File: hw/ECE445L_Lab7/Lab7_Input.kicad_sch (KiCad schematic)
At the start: 5 parts, among them SW1 UP, SW2 DOWN, SW3 LEFT, SW4 RIGHT, SW5 MODE

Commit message: Updated hardware schematic
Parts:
- added R44, R45, R46, R47, R48: 10k, symbol Device:R
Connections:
- net SW_DOWN renamed PB1
- net PB1: now also R45.2
- net SW_LEFT renamed PB2
- net PB2: now also R46.2
- net SW_MODE renamed PB4
- net PB4: now also R48.2
- net SW_RIGHT renamed PB3
- net PB3: now also R47.2
- net SW_UP renamed PB0
- net PB0: now also R44.2
- new net +3V3: R44.1, R45.1, R46.1, R47.1, R48.1
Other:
- moved on the sheet: SW1, SW2, SW3, SW4, SW5

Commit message: More Updates to hardware
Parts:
- added R49, R50, R51, R52, R53, R54, R55: 10k, ECE445L:Potentiometer, symbol ECE445L:Potentiometer
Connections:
- net +3V3: now also R49.1, R50.1, R51.1, R52.1, R53.1, R54.1, R55.1
- net GND: now also R49.3, R50.3, R51.3, R52.3, R53.3, R54.3, R55.3
- new net PE1: R51.2, R52.2, R53.2, R54.2, R55.2
- new net PE2: R50.2
- new net PE3: R49.2
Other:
- note added: "Bass"
- note added: "Distortion Knob"
- note added: "Flanger Potentiometers"
- note added: "Mid"
- note added: "Treble"
- note added: "Volume"

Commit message: Lab7A Schematic and BOM - Ashton
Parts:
- added R80: 10k, ECE445L:Potentiometer, symbol ECE445L:Potentiometer
- added R81: 10k, symbol Device:R
- added SW6: Delay, ECE445L:SW_PUSH_6mm, symbol ECE445L:SW_Push
- SW1: value UP -> Pause
- SW2: value DOWN -> LCDMode
- SW3: value LEFT -> Flanger
- SW4: value RIGHT -> Distortion
- SW5: value MODE -> Reverb
- renumbered R44 to R65, R45 to R66, R46 to R67, R47 to R68, R48 to R69, R49 to R70, R50 to R71, R51 to R72, R52 to R73, R53 to R74, R54 to R75, R55 to R76
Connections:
- net +3V3: now also R80.1, R81.1
- net GND: now also R80.3, SW6.1
- net PE1: no longer R73.2, R74.2, R75.2, R76.2
- new net PC7: R81.2, SW6.2
- new net PD1: R76.2, R80.2
- new net PD2: R75.2
- new net PD3: R74.2
- new net PE0: R73.2
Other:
- note added: "Delay"

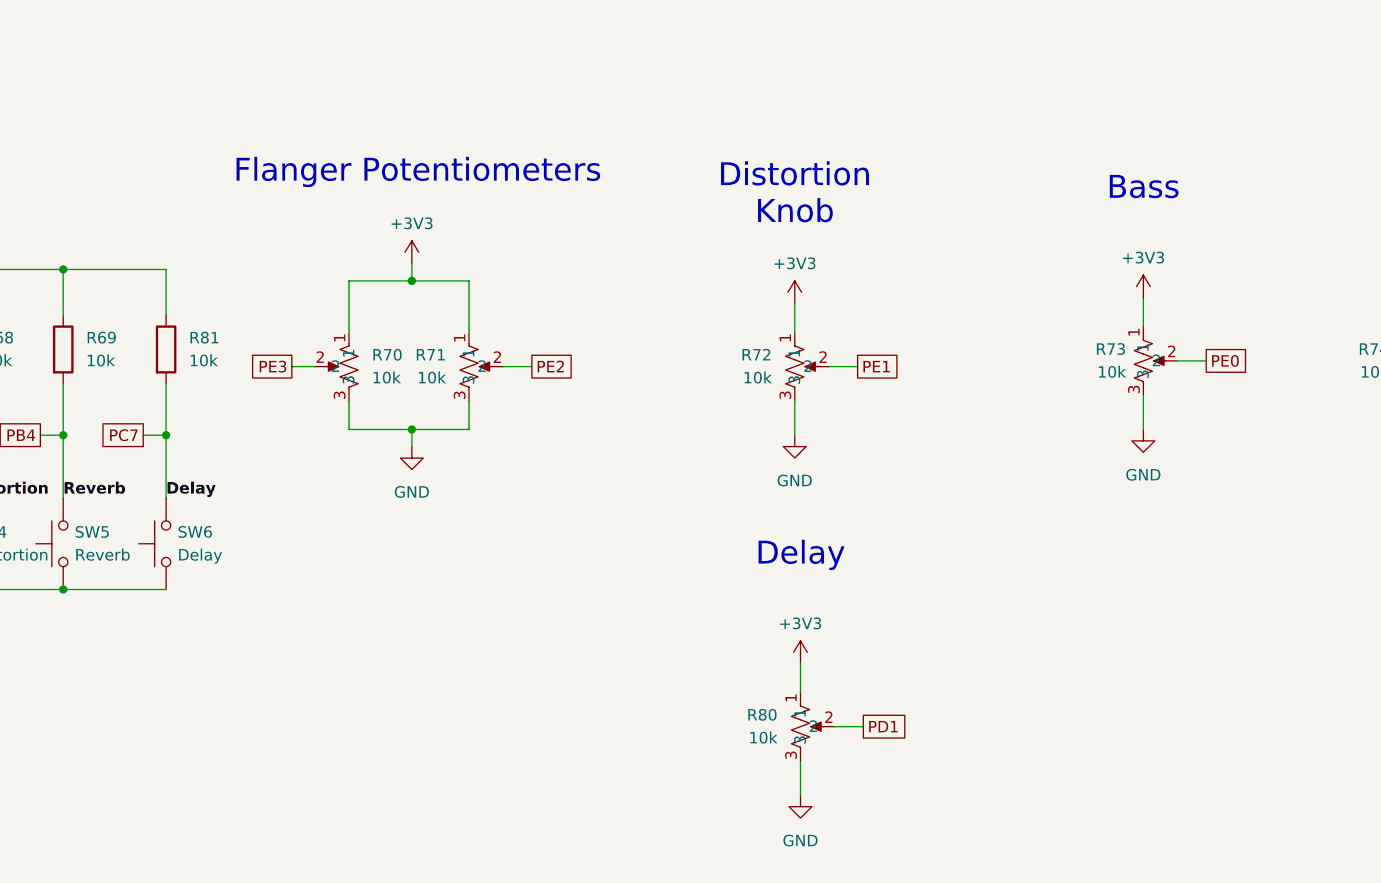
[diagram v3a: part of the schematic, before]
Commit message: Made changers to the schematic, updated bom, and created priliminary layout for the PCB. Ready for 7B Prep!
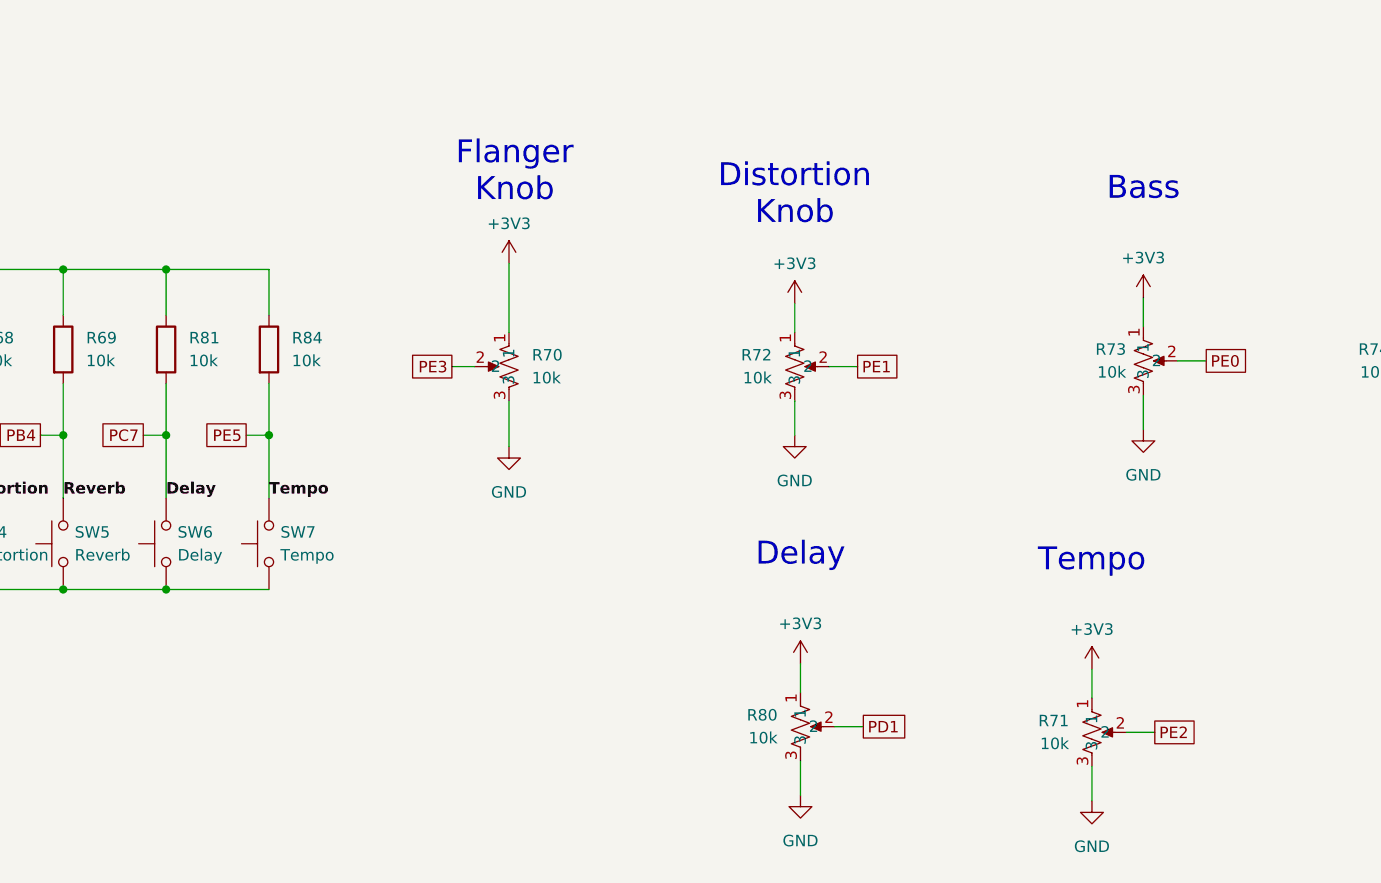
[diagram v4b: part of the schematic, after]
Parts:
- added R84: 10k, Resistor_SMD:R_0603_1608Metric, symbol Device:R
- added SW7: Tempo, ECE445L:SW_PUSH_6mm, symbol ECE445L:SW_Push
- R65, R66, R67, R68, R69, R81: footprint (none) -> Resistor_SMD:R_0603_1608Metric
- R70, R71, R72, R73, R74, R75, R76, R80: footprint ECE445L:Potentiometer -> ECE445L:P120PK-Y25BR10K
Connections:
- net +3V3: now also R84.1
- net GND: now also SW7.1
- new net PE5: R84.2, SW7.2
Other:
- note added: "Flanger Knob"
- note added: "Tempo"
- note removed: "Flanger Potentiometers"
- moved on the sheet: R70, R71

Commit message: Rough draft layout - need to remove tm4c chip
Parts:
- R70: renamed from R65; footprint Resistor_SMD:R_0603_1608Metric -> Resistor_SMD:R_0603_1608Metric_Pad0.98x0.95mm_HandSolder
- R71: renamed from R66; footprint Resistor_SMD:R_0603_1608Metric -> Resistor_SMD:R_0603_1608Metric_Pad0.98x0.95mm_HandSolder
- R72: renamed from R67; footprint Resistor_SMD:R_0603_1608Metric -> Resistor_SMD:R_0603_1608Metric_Pad0.98x0.95mm_HandSolder
- R73: renamed from R68; footprint Resistor_SMD:R_0603_1608Metric -> Resistor_SMD:R_0603_1608Metric_Pad0.98x0.95mm_HandSolder
- R74: renamed from R69; footprint Resistor_SMD:R_0603_1608Metric -> Resistor_SMD:R_0603_1608Metric_Pad0.98x0.95mm_HandSolder
- R75: renamed from R81; footprint Resistor_SMD:R_0603_1608Metric -> Resistor_SMD:R_0603_1608Metric_Pad0.98x0.95mm_HandSolder
- R76: renamed from R84; footprint Resistor_SMD:R_0603_1608Metric -> Resistor_SMD:R_0603_1608Metric_Pad0.98x0.95mm_HandSolder
- renumbered R70 to R77, R72 to R78, R80 to R79, R71 to R80, R73 to R81, R74 to R82, R75 to R83, R76 to R84, SW1 to SW2, SW2 to SW3, SW3 to SW4, SW4 to SW5, SW5 to SW6, SW6 to SW7, SW7 to SW8
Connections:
- net PD1: no longer R79.2
- net PB0 renamed PF0
- net PB1 renamed PF1
- net PB2 renamed PF2
- net PB3 renamed PF3
- net PB4 renamed PF4
- new net PE4: R79.2
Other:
- company: (none) -> The University of Texas at Austin
- title: (none) -> ECE 445L Lab7

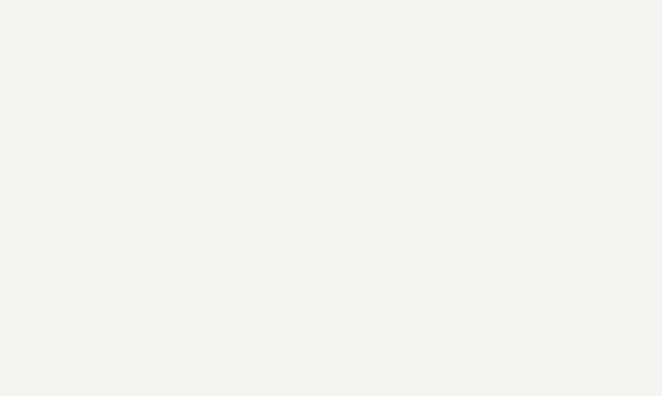
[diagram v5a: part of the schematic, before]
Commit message: Added current consumption to schematic
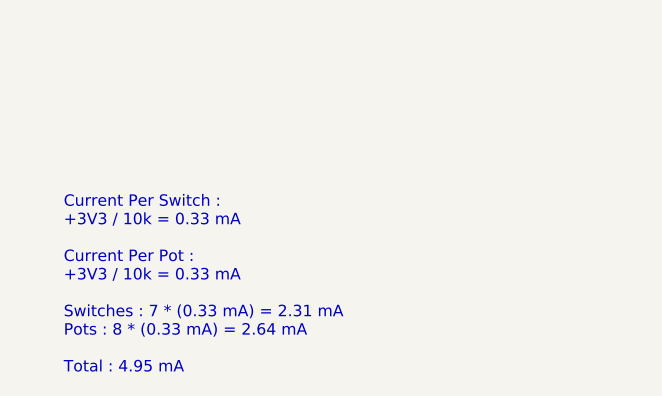
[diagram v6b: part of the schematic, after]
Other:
- note added: "Current Per Switch : +3V3 / 10k = 0.33 mA Current Per Pot : +3V3 / 10k = 0.33 mA Switches : 7 * (0.33 mA) = 2.31 mA Pots : 8 * (0.33 mA) = 2.64 mA Total : 4.95 mA"
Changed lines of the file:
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@@
 		(comment 1 "Drawn By Ashton Knecht - atk836")
+	)
+	(text "Current Per Switch :\n+3V3 / 10k = 0.33 mA\n\nCurrent Per Pot :\n+3V3 / 10k = 0.33 mA\n\nSwitches : 7 * (0.33 mA) = 2.31 mA\nPots : 8 * (0.33 mA) = 2.64 mA\n\nTotal : 4.95 mA"
+		(exclude_from_sim no)
+		(at 36.195 182.88 0)
+		(effects
+			(font
+				(size 1.27 1.27)
+			)
+			(justify left)
+		)
 	)
 	(text "Mid"

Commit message: Updated lab7a report
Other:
- note added: "Inputs Current Consumption Current Per Switch : +3V3 / 10k = 0.33 mA Current Per Pot : +3V3 / 10k = 0.33 mA Switches : 7 * (0.33 mA) = 2.31 mA Pots : 8 * (0.33 mA) = 2.64 mA Total : 4.95 mA"
- note removed: "Current Per Switch : +3V3 / 10k = 0.33 mA Current Per Pot : +3V3 / 10k = 0.33 mA Switches : 7 * (0.33 mA) = 2.31 mA Pots : 8 * (0.33 mA) = 2.64 mA Total : 4.95 mA"
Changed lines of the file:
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@@
 		(comment 1 "Drawn By Ashton Knecht - atk836")
 	)
-	(text "Current Per Switch :\n+3V3 / 10k = 0.33 mA\n\nCurrent Per Pot :\n+3V3 / 10k = 0.33 mA\n\nSwitches : 7 * (0.33 mA) = 2.31 mA\nPots : 8 * (0.33 mA) = 2.64 mA\n\nTotal : 4.95 mA"
+	(text "Inputs Current Consumption\n\nCurrent Per Switch :\n+3V3 / 10k = 0.33 mA\n\nCurrent Per Pot :\n+3V3 / 10k = 0.33 mA\n\nSwitches : 7 * (0.33 mA) = 2.31 mA\nPots : 8 * (0.33 mA) = 2.64 mA\n\nTotal : 4.95 mA"
 		(exclude_from_sim no)
 		(at 36.195 182.88 0)

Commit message: PCB Layout
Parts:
- added C10, C4, C5, C6, C7, C8, C9: 0.1u, Capacitor_SMD:C_0603_1608Metric_Pad1.08x0.95mm_HandSolder, symbol ECE445L:C
- added R89, R91, R93, R95: 100, Resistor_SMD:R_0603_1608Metric_Pad0.98x0.95mm_HandSolder, symbol Device:R
- added R90, R92, R94: 100k, Resistor_SMD:R_0603_1608Metric_Pad0.98x0.95mm_HandSolder, symbol Device:R
- R70, R71, R73, R75: value 10k -> 100k
- R72, R74, R76: value 10k -> 100
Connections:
- net +3V3: now also R90.1, R92.1, R94.1; no longer R72.1, R74.1, R76.1
- net GND: now also C10.1, C4.1, C5.1, C6.1, C7.1, C8.1, C9.1
- net PC7: now also C9.2, R93.2; no longer R75.2, SW7.2
- net PE5: now also C10.2, R95.2; no longer R76.2, SW8.2
- net PF0: now also C4.2, R89.2; no longer R70.2, SW2.2
- net PF1: now also R72.2, C5.2; no longer R71.2, SW3.2
- net PF2: now also R74.2, C6.2; no longer R72.2, SW4.2
- net PF3: now also R76.2, C7.2; no longer R73.2, SW5.2
- net PF4: now also C8.2, R91.2; no longer R74.2, SW6.2
- new net Delay: R92.2, R93.1, SW7.2
- new net Distortion: R75.2, R76.1, SW5.2
- new net Flanger: R73.2, R74.1, SW4.2
- new net LCDMode: R71.2, R72.1, SW3.2
- new net Pause: R70.2, R89.1, SW2.2
- new net Reverb: R90.2, R91.1, SW6.2
- new net Tempo: R94.2, R95.1, SW8.2
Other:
- note added: "Changed For Low Pass Filter"
- moved on the sheet: R70, R77, R78, R79, R80, R81, R82, R83, R84, SW2
